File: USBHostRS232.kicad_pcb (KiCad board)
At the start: 2 copper layers, 50 x 79 mm, 50 parts, among them J2 DB9_Male, J4 USB_A, J5 5V_IN, Q1 SI2301CDS-T1-GE3, SW1 PROG, SW2 RST, U1 MAX3232, U2 CH559L, U3 XC6206, U4 USBLC6-2SC6

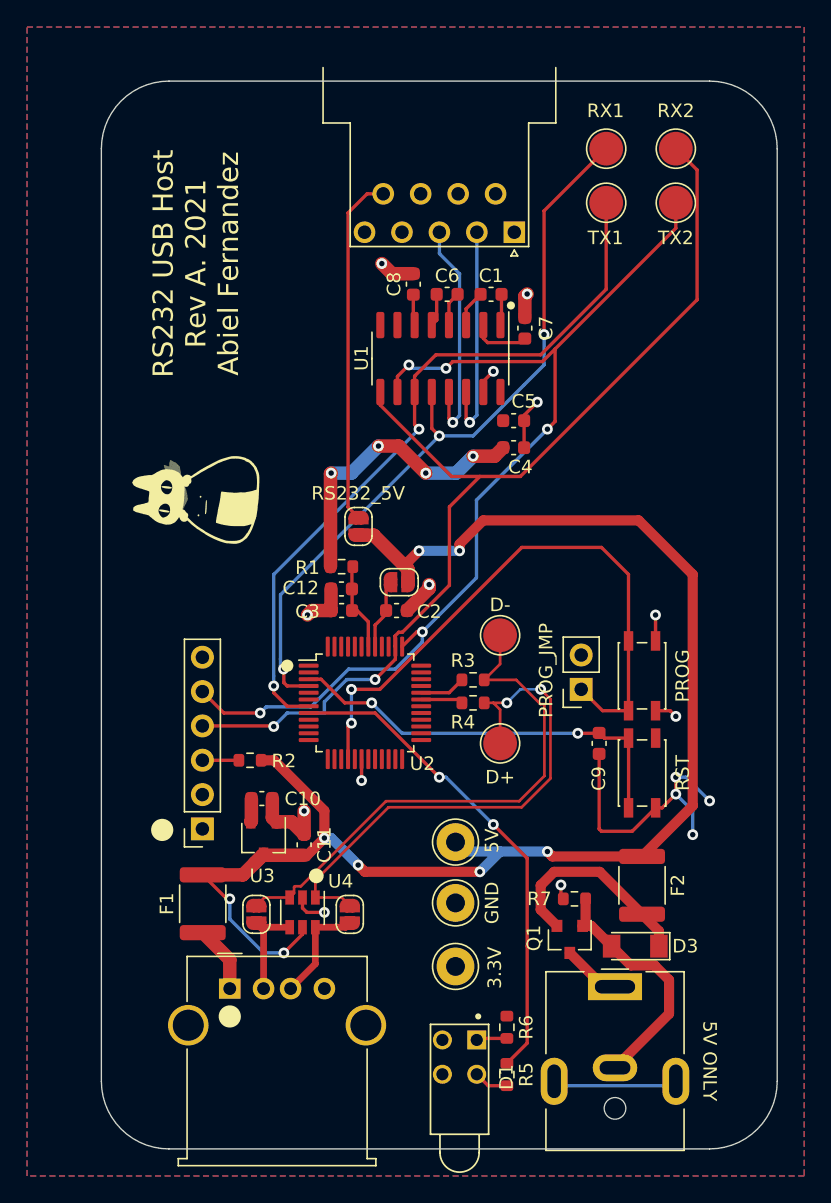
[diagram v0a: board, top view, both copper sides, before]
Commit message: Added mounting holes
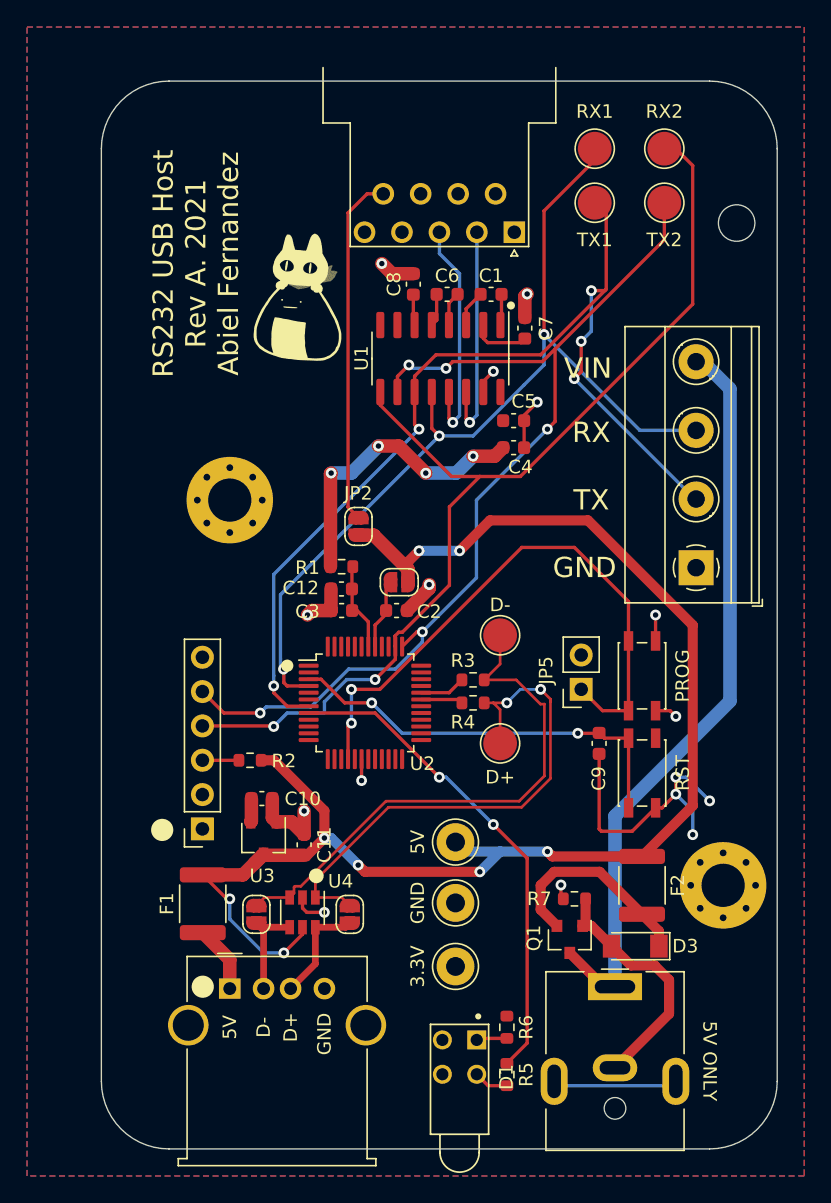
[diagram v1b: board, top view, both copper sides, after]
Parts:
- added J6: Screw_Terminal_01x04, TerminalBlock_Phoenix:TerminalBlock_Phoenix_MKDS-1,5-4-5.08_1x04_P5.08mm_Horizontal, F.Cu at (149.5, 85.0)
- added REF**: MountingHole_2.7mm_M2.5, MountingHole:MountingHole_2.7mm_M2.5, F.Cu at (152.5, 59.5)
- added REF**: MountingHole_3.2mm_M3_Pad_Via, MountingHole:MountingHole_3.2mm_M3_Pad_Via, F.Cu at (115.0, 80.0)
- added REF**: MountingHole_3.2mm_M3_Pad_Via, MountingHole:MountingHole_3.2mm_M3_Pad_Via, F.Cu at (151.5, 108.5)
- moved G*** 16.8 mm to (120.0, 65.0), turned to 0 degrees
- moved TP1 0.85 mm to (142.0, 54.0)
- moved TP2 0.85 mm to (142.0, 58.0)
- moved TP3 0.85 mm to (147.2, 54.0)
- moved TP4 0.85 mm to (147.2, 58.0)
- renumbered RS232_5V to JP2, PROG_JMP to JP5, RX1 to TP1, TX1 to TP2, RX2 to TP3, TX2 to TP4, 3.3V to TP5, 5V to TP6, GND to TP7
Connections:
- net Net-(J5-Pad1) renamed VIN
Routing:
- net VIN: track 4.38 -> 55.0 mm
- net TX_1: track 54.3 -> 75.5 mm, vias 2 -> 5
- net RX_1: track 56.5 -> 71.2 mm
- net +5V: track 113.8 -> 111.3 mm
- net PROG: track 45.2 -> 44.0 mm
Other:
- board text added: "VIN"
